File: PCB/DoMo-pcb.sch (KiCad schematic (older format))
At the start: 32 parts, among them SW0 SW_Push, SW1 Rotary_Encoder_Switch, SW10 SW_Push, SW2 SW_Push, SW3 SW_Push, SW4 SW_Push, SW5 SW_Push, SW6 SW_Push, SW7 SW_Push, SW8 SW_Push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

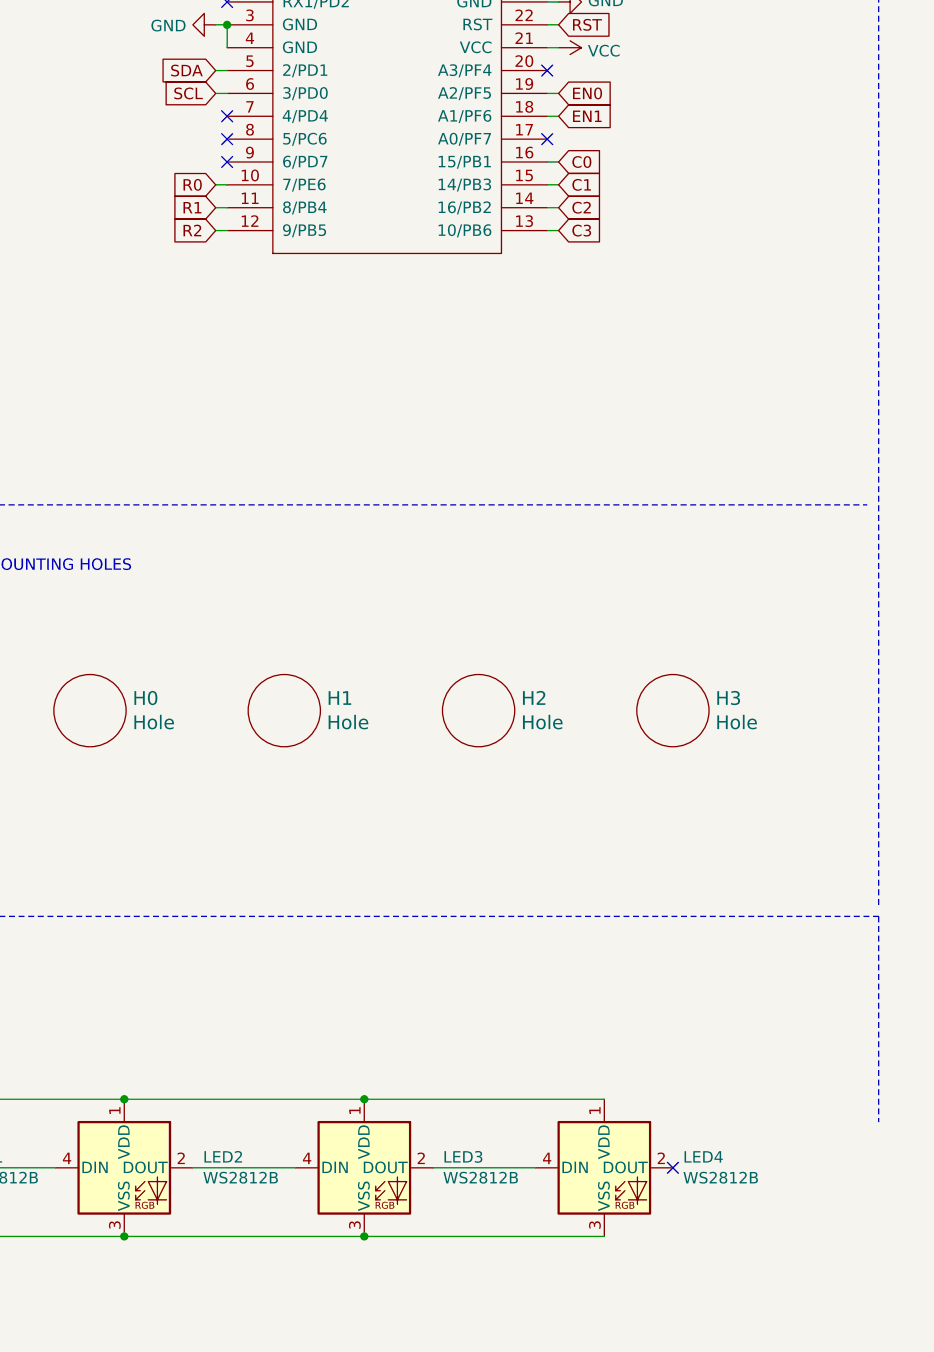
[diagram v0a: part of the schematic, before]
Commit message: remove 1 led and wire up oled/rotary
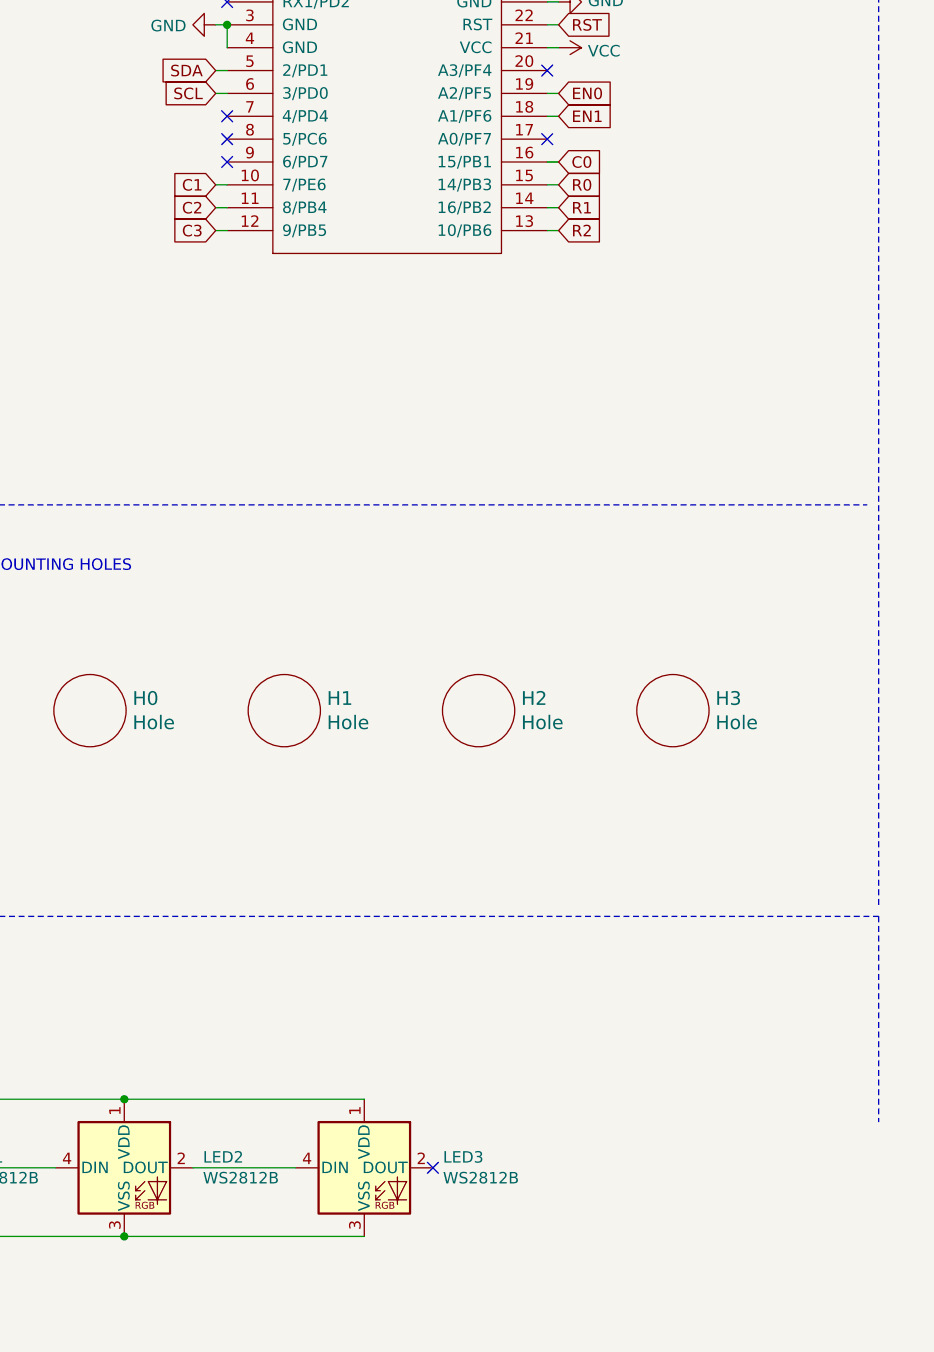
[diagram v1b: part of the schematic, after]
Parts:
- removed LED4: WS2812B, LEDs:LED_WS2812B-PLCC4, symbol LED:WS2812B
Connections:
- net C1: now also U0.10 (7/PE6); no longer U0.15 (14/PB3)
- net C2: now also U0.11 (8/PB4); no longer U0.14 (16/PB2)
- net C3: now also U0.12 (9/PB5); no longer U0.13 (10/PB6)
- net R0: now also U0.15 (14/PB3); no longer U0.10 (7/PE6)
- net R1: now also U0.14 (16/PB2); no longer U0.11 (8/PB4)
- net R2: now also U0.13 (10/PB6); no longer U0.12 (9/PB5)
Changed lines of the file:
@@
-	1    0    0    -1
-$EndComp
-$Comp
-L LED:WS2812B LED3
-U 1 1 5F05ECBC
-P 4700 6750
-F 0 "LED3" H 5044 6796 50  0000 L CNN
-F 1 "WS2812B" H 5044 6705 50  0000 L CNN
-F 2 "LEDs:LED_WS2812B-PLCC4" H 4750 6450 50  0001 L TNN
-F 3 "https://cdn-shop.adafruit.com/datasheets/WS2812B.pdf" H 4800 6375 50  0001 L TNN
-	1    4700 6750
-	1    0    0    -1
-$EndComp
-$Comp
-L LED:WS2812B LED4
-U 1 1 5F05F745
-P 5750 6750
-F 0 "LED4" H 6094 6796 50  0000 L CNN
-F 1 "WS2812B" H 6094 6705 50  0000 L CNN
-F 2 "LEDs:LED_WS2812B-PLCC4" H 5800 6450 50  0001 L TNN
-F 3 "https://cdn-shop.adafruit.com/datasheets/WS2812B.pdf" H 5850 6375 50  0001 L TNN
-	1    5750 6750
 	1    0    0    -1
 $EndComp
@@
 Wire Wire Line
 	2900 6750 3350 6750
-Wire Wire Line
-	3950 6750 4400 6750
-Wire Wire Line
-	5000 6750 5450 6750
-NoConn ~ 6050 6750
 $Comp
 L power:GND #PWR0103
@@
 $EndComp
 Wire Wire Line
-	5750 7050 4700 7050
-Wire Wire Line
-	3650 7050 4700 7050
-Connection ~ 4700 7050
-Wire Wire Line
 	3650 7050 2600 7050
 Wire Wire Line
@@
 Wire Wire Line
 	2600 7050 1550 7050
-Wire Wire Line
-	5750 6450 4700 6450
 Connection ~ 2600 6450
 Wire Wire Line
@@
 Wire Wire Line
 	3650 6450 2600 6450
-Connection ~ 4700 6450
-Wire Wire Line
-	4700 6450 3650 6450
 $Comp
 L power:VCC #PWR0104
@@
 	2850 3850 6900 3850
 NoConn ~ 5500 2250
-NoConn ~ 4100 2350
-NoConn ~ 4100 2250
-NoConn ~ 4100 2150
 NoConn ~ 4100 1650
 NoConn ~ 5500 1550
@@
 Wire Wire Line
 	4100 1550 4050 1550
-Text GLabel 5550 2550 2    50   Input ~ 0
+Text GLabel 4050 2550 0    50   Input ~ 0
 C2
-Text GLabel 5550 2450 2    50   Input ~ 0
+Text GLabel 4050 2450 0    50   Input ~ 0
 C1
-Text GLabel 5550 2350 2    50   Input ~ 0
-C0
 Wire Wire Line
 	4100 2650 4050 2650
 Wire Wire Line
 	4100 2550 4050 2550
-Text GLabel 4050 2650 0    50   Input ~ 0
-R2
-Text GLabel 4050 2550 0    50   Input ~ 0
-R1
 Wire Wire Line
 	4100 2450 4050 2450
-Text GLabel 4050 2450 0    50   Input ~ 0
-R0
 Wire Wire Line
 	5550 2150 5500 2150
@@
 Wire Wire Line
 	4100 1950 4050 1950
-Text GLabel 4050 1950 0    50   Input ~ 0
-SDA
 Connection ~ 4100 1750
 Wire Wire Line
@@
 	1    0    0    -1
 $EndComp
-Text GLabel 5550 2650 2    50   Input ~ 0
+Text GLabel 4050 2650 0    50   Input ~ 0
 C3
-Wire Wire Line
-	5550 2350 5500 2350
-Wire Wire Line
-	5550 2450 5500 2450
-Wire Wire Line
-	5550 2550 5500 2550
 Wire Wire Line
 	5500 2650 5550 2650
@@
 	1    0    0    -1
 $EndComp
+Text GLabel 4050 1950 0    50   Input ~ 0
+SDA
+Wire Wire Line
+	5550 2450 5500 2450
+Wire Wire Line
+	5550 2550 5500 2550
+Text GLabel 5550 2650 2    50   Input ~ 0
+R2
+Text GLabel 5550 2550 2    50   Input ~ 0
+R1
+Text GLabel 5550 2450 2    50   Input ~ 0
+R0
+NoConn ~ 4100 2250
+NoConn ~ 4100 2150
+Text GLabel 5550 2350 2    50   Input ~ 0
+C0
+Wire Wire Line
+	5500 2350 5550 2350
+NoConn ~ 4100 2350
+Wire Wire Line
+	3950 6750 4400 6750
+Wire Wire Line
+	4700 6450 3650 6450
+Wire Wire Line
+	3650 7050 4700 7050
+$Comp
+L LED:WS2812B LED3
+U 1 1 5F05ECBC
+P 4700 6750
+F 0 "LED3" H 5044 6796 50  0000 L CNN
+F 1 "WS2812B" H 5044 6705 50  0000 L CNN
+F 2 "LEDs:LED_WS2812B-PLCC4" H 4750 6450 50  0001 L TNN
+F 3 "https://cdn-shop.adafruit.com/datasheets/WS2812B.pdf" H 4800 6375 50  0001 L TNN
+	1    4700 6750
+	1    0    0    -1
+$EndComp
+NoConn ~ 5000 6750
 $EndSCHEMATC
